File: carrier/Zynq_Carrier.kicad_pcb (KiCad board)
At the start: 4 copper layers, 148 x 137 mm, 538 parts, among them J11001 Header_2x20_2.54mm, J12001 HDMI-019S, J14001 HDMI-019S, J15001 AFC07-S40FCA-00, J16001 TF-01A, J17001 TYPE-C-31-M-12, J18001 DS1024-2x6R2, J18002 DS1024-2x6R2, J19001 DS1024-2x6R2, J2001 ZX-SH1.0-4PWT, J23001 KH-5224-8P8C-D, J24001 DF40C-100DS-0.4V(51), J25002 DF40C-100DS-0.4V(51), J26003 DF40C-100DS-0.4V(51), J29001 TYPE-C-31-M-12, J31001 TYPE-C-31-M-12, J32002 TYPE-C-31-M-12, J8001 SFW15R-1STE1LF, J9001 878311420, J9002 HX_JN1.27-2x5, Q20001 AO3400A, SW1001 DSHP04TSGER, SW19001 DSHP04TSGER, SW28001 DSHP04TSGER, SW33001 USER, SW33002 USER, SW33003 USER, SW33004 USER, SW7001 DSHP04TSGER, SW7002 DSHP08TSGER, SW7003 TS-1187A-B-A-B, SW7004 TS-1187A-B-A-B, SW7005 TS-1187A-B-A-B, SW7006 DSHP04TSGER, SW9001 DIP-4, SW9002 RESET, T10001 HX5008NLT, U1001 SY6280AAC, U1002 PCA9306DCUR, U11001 TLV75725PDYDR, U12001 M24C02-WMN6TP, U12002 TPD4E02B04DQAR, U12003 TPD4E02B04DQAR, U12004 TPD4E05U06DQAR, U14001 TPD12S016PWR, U15001 SY7201ABC, U15002 USBLC6-2SC6, U16001 TXS02612RTWR, U16002 TPD6E001RSER, U17001 TPS26631PWPR, U17002 USBLC6-2SC6, U18001 TPD4E1U06, U18002 TPD4E1U06, U18003 TPD4E1U06, U18004 TPD4E1U06, U19001 SY6280AAC, U19002 TPD4E1U06, U19003 TPD4E1U06, U20001 LM61460AANRJRR, U20002 LM61460AANRJRR, U20003 AP2112K-1.8, U2001 USBLC6-2SC6, U21001 INA3221AIRGVR, U21002 INA3221AIRGVR, U22004 LM61460AANRJRR, U27001 CP2102N-A02, U28001 CH347T, U28002 SN74LVC125ADR, U28004 AP2112K-3.3TRG1, U29001 USBLC6-2SC6, U30001 FUSB302BMPX, U3001 24AA025E48T-I/OT, U3002 RV-3028-C7-32.768kHz-1ppm-TA-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, U3003 TPS3823-33DBVR, U31001 USBLC6-2SC6, U32001 TPS2051CDBVR, U32002 USBLC6-2SC6, U4001 SN74LVC1G08, U4002 SN74LVC1G08, U4003 SN74LVC1G08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

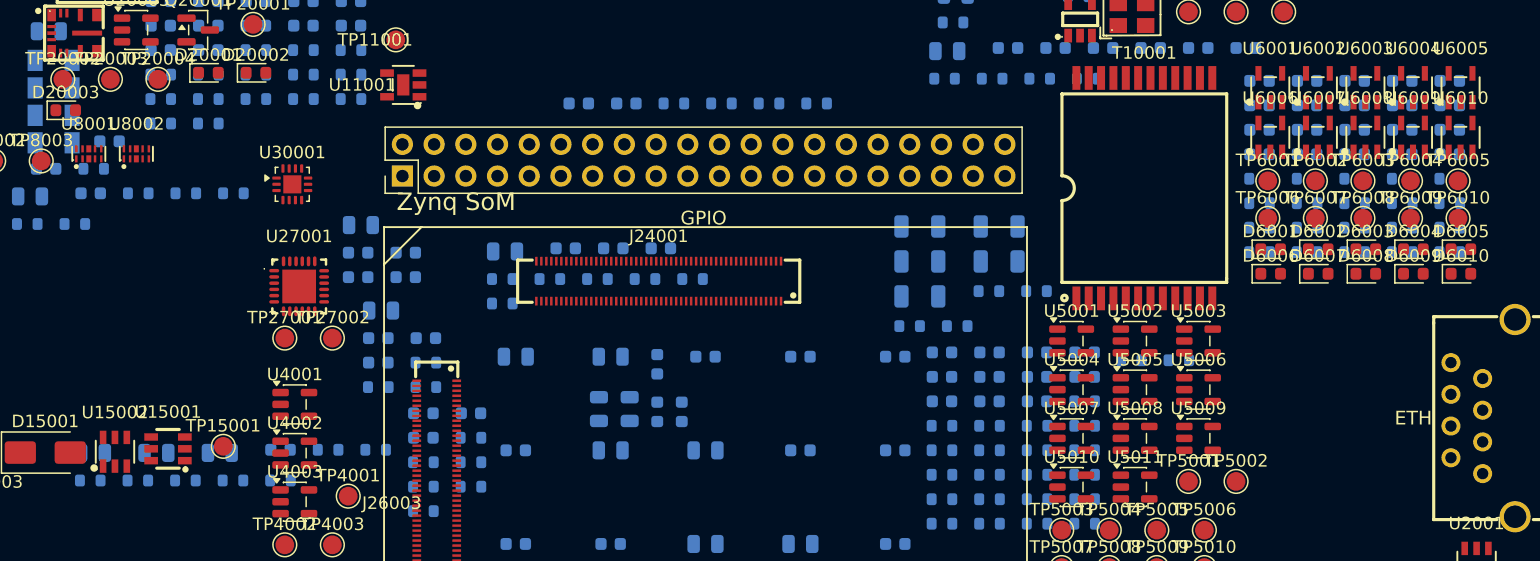
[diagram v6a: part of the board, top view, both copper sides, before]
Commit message: fix(audit round-3 / verification pass): regression revert + 6 gaps the re-audit caught
A second independent 65-agent audit of the REMEDIATED board confirmed ZERO
CRITICAL/HIGH (the 3 board-dead fixes held) and surfaced a regression + gaps:

REGRESSION I introduced (caught by re-verify): power_som R18 RT comment said
"~1.5 MHz" — WRONG. RT=22k sets ~600 kHz (SNVSBD5D Eq 2), corroborated by the
folder's own README:43 and the sibling LM61460 cells. I had trusted the FIRST
audit's RT claim; the second audit + the README prove it backwards. Reverted to
600 kHz (resistor value 22k was always correct).

Gaps closed (real):
- lcd: add the dossier-specified 1uF HF bypass (C15849) at the SY7201 boost IN
  (only the 10u bulk was placed). +.cir +test.
- bringup_modules: add a 10k bleed on +3V3_SD (research R5) — SY6280 has no QOD, so
  the SD rail needs a discharge path for power-cycle re-init. +.cir.
- camera: clamp CAM_SCL/CAM_SDA on U2's two SPARE ESD channels (free GND-ref TVS on
  the user-handled FFC I2C lines); CAM_EN/LED stay static-GPIO (documented). +test.
- ratings.py: add the TPD4E1U06 (C124691) TVS row (was UNSPEC fail-soft).
- powertree: remove the dead 'TPS54302' REG_SPECS key (no emitted part uses it,
  BOM-verified) + fix its stale parallel-source comments to LM61460.
- stale docs: bringup_en/.py+README + bringup_en_modules (TPS54302->LM61460 EN),
  rj45 +VLED rationale (the always-on +3V3_SC DOES exist) + README mounting holes,
  som_j2 README (retired FMC_PRSNT_N).

Verified: 148x137, DRC 0, BOARD PASS, POWER TREE PASS (0 findings), golden blessed;
lcd+camera+bringup_modules tests 61/61.

Co-Authored-By: Claude Opus 4.8 <noreply@anthropic.com>
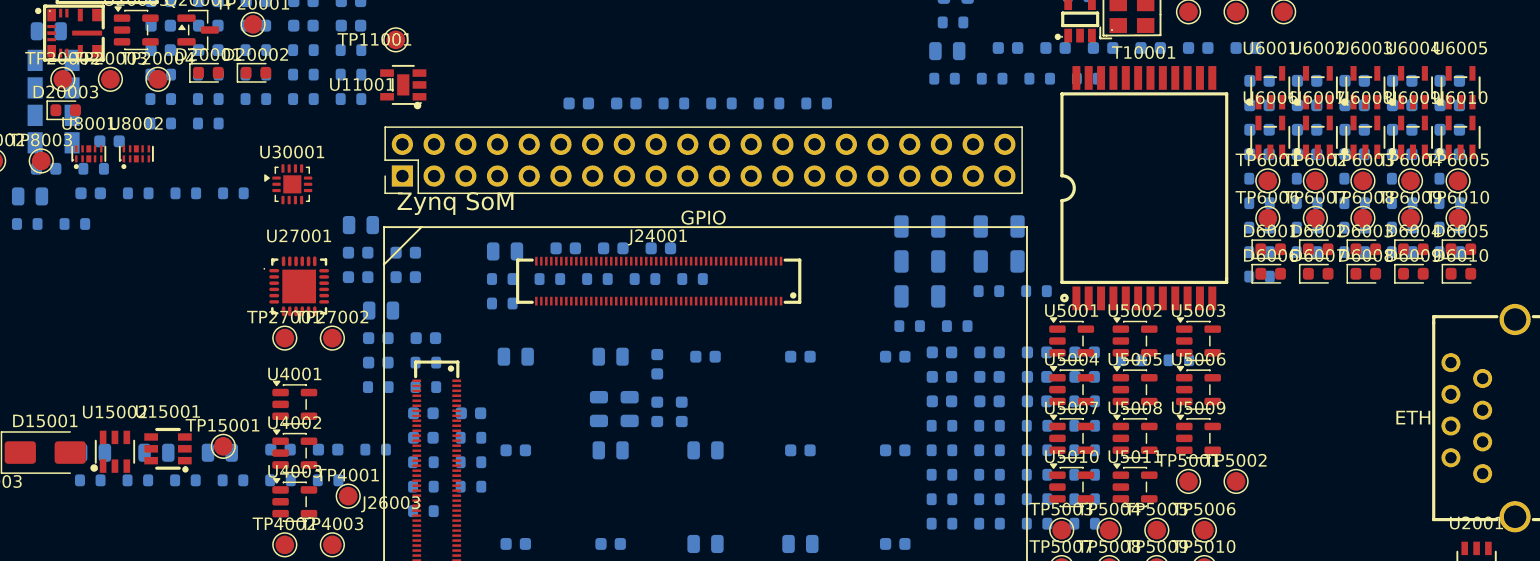
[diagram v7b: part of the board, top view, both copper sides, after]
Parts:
- added C15005: 1u, Capacitor_SMD:C_0603_1608Metric, B.Cu at (68.8, 89.7)
- added R6021: 10k, Resistor_SMD:R_0603_1608Metric, B.Cu at (143.4, 75.8)
- moved R15002 23.0 mm to (49.7, 92.2)
- moved R15001 3.81 mm to (72.6, 89.7)
- moved R15004 3.81 mm to (57.3, 92.2)
- moved R15006 3.81 mm to (65.0, 92.2)
- moved R15003 3.81 mm to (53.5, 92.2)
- moved R15005 3.81 mm to (61.1, 92.2)
- moved R15007 3.81 mm to (68.8, 92.2)
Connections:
- U8002 pad 4: (no net) -> CAM_SCL
- U8002 pad 5: (no net) -> CAM_SDA
